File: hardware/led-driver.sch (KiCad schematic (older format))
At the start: 8 parts, among them Q1 BC547

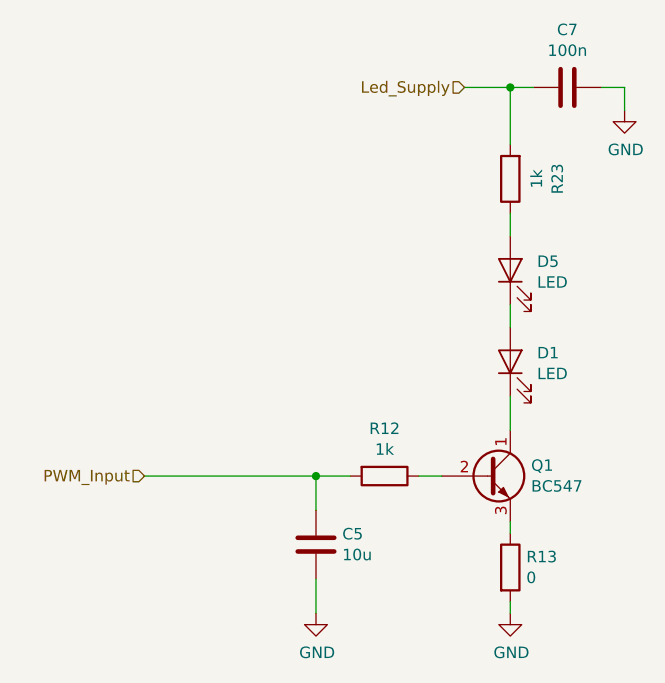
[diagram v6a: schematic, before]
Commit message: Fix relais supply
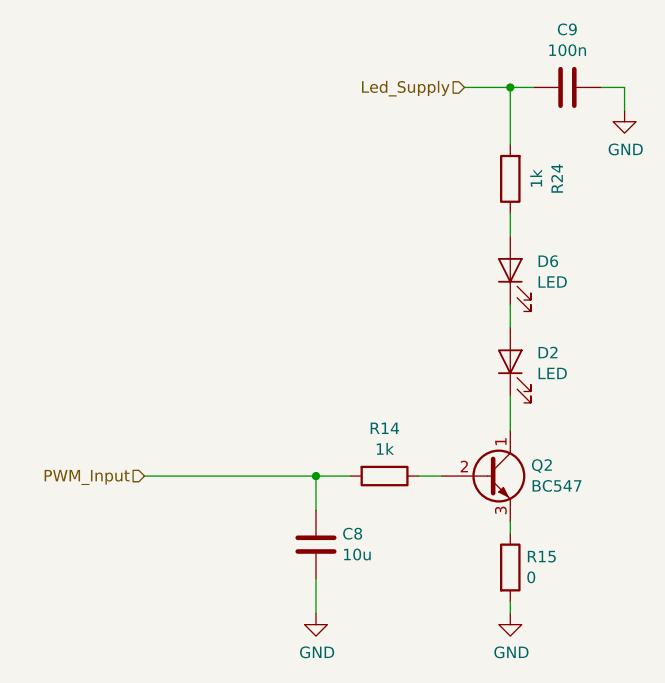
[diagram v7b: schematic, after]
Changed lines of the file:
@@
 $Descr A4 11693 8268
 encoding utf-8
-Sheet 2 5
+Sheet 3 5
 Title ""
 Date ""
@@
 AR Path="/5C8EC687/5C8EC7F4" Ref="Q1"  Part="1"
 AR Path="/5C8EFAFF/5C8EC7F4" Ref="Q2"  Part="1"
-F 0 "Q1" H 4341 3146 50  0000 L CNN
+F 0 "Q2" H 4341 3146 50  0000 L CNN
 F 1 "BC547" H 4341 3055 50  0000 L CNN
 F 2 "Package_TO_SOT_THT:TO-92_Inline" H 4350 3025 50  0001 L CIN
@@
 AR Path="/5C8EC687/5C8EC98B" Ref="D1"  Part="1"
 AR Path="/5C8EFAFF/5C8EC98B" Ref="D2"  Part="1"
-F 0 "D1" V 4288 2483 50  0000 R CNN
+F 0 "D2" V 4288 2483 50  0000 R CNN
 F 1 "LED" V 4197 2483 50  0000 R CNN
 F 2 "LED_SMD:LED_0805_2012Metric" H 4250 2600 50  0001 C CNN
@@
 AR Path="/5C8EC687/5C8ECB18" Ref="R13"  Part="1"
 AR Path="/5C8EFAFF/5C8ECB18" Ref="R15"  Part="1"
-F 0 "R13" H 4320 3546 50  0000 L CNN
+F 0 "R15" H 4320 3546 50  0000 L CNN
 F 1 "0" H 4320 3455 50  0000 L CNN
 F 2 "Resistor_SMD:R_0805_2012Metric_Pad1.15x1.40mm_HandSolder" V 4180 3500 50  0001 C CNN
@@
 AR Path="/5C8EC687/5C8ECBDB" Ref="R12"  Part="1"
 AR Path="/5C8EFAFF/5C8ECBDB" Ref="R14"  Part="1"
-F 0 "R12" V 3493 3100 50  0000 C CNN
+F 0 "R14" V 3493 3100 50  0000 C CNN
 F 1 "1k" V 3584 3100 50  0000 C CNN
 F 2 "Resistor_SMD:R_0805_2012Metric_Pad1.15x1.40mm_HandSolder" V 3630 3100 50  0001 C CNN
@@
 AR Path="/5C8EC687/5C8ECCDD" Ref="C7"  Part="1"
 AR Path="/5C8EFAFF/5C8ECCDD" Ref="C9"  Part="1"
-F 0 "C7" V 4248 1400 50  0000 C CNN
+F 0 "C9" V 4248 1400 50  0000 C CNN
 F 1 "100n" V 4339 1400 50  0000 C CNN
 F 2 "Capacitor_SMD:C_0805_2012Metric_Pad1.15x1.40mm_HandSolder" H 4538 1250 50  0001 C CNN
@@
 AR Path="/5C8EC687/5C8ECE43" Ref="C5"  Part="1"
 AR Path="/5C8EFAFF/5C8ECE43" Ref="C8"  Part="1"
-F 0 "C5" H 3285 3354 50  0000 R CNN
+F 0 "C8" H 3285 3354 50  0000 R CNN
 F 1 "10u" H 3285 3445 50  0000 R CNN
 F 2 "Capacitor_SMD:C_0805_2012Metric_Pad1.15x1.40mm_HandSolder" H 3438 3250 50  0001 C CNN
@@
 AR Path="/5C8EC687/5CD989FA" Ref="D5"  Part="1"
 AR Path="/5C8EFAFF/5CD989FA" Ref="D6"  Part="1"
-F 0 "D5" V 4288 2083 50  0000 R CNN
+F 0 "D6" V 4288 2083 50  0000 R CNN
 F 1 "LED" V 4197 2083 50  0000 R CNN
 F 2 "LED_SMD:LED_0805_2012Metric" H 4250 2200 50  0001 C CNN
@@
 AR Path="/5C8EC687/5CD998D9" Ref="R23"  Part="1"
 AR Path="/5C8EFAFF/5CD998D9" Ref="R24"  Part="1"
-F 0 "R23" V 4043 1800 50  0000 C CNN
+F 0 "R24" V 4043 1800 50  0000 C CNN
 F 1 "1k" V 4134 1800 50  0000 C CNN
 F 2 "Resistor_SMD:R_0805_2012Metric_Pad1.15x1.40mm_HandSolder" V 4180 1800 50  0001 C CNN
